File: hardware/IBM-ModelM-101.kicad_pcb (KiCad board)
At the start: 2 copper layers, 150 x 50 mm, 44 parts, among them J1 CONN-MOLEX-0670688000-USB-B, J2 KEYBOARD_ACTIVE_LINES, J3 KEYBOARD_INPUT_LINES, J4 CHASSIS_GROUND, J5 STATUS_LEDS, J6 DEBUG_FTDI, J7 JTAG, SW1 BOOT0, SW2 RESET, U1 TLV70233DBV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

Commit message: Adjusted output gerber naming
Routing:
- net GND: track 40.4 -> 33.1 mm
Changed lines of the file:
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@@
     (thickness 1.6)
     (drawings 93)
-    (tracks 501)
+    (tracks 499)
     (zones 0)
     (modules 44)
@@
   (page A4)
   (layers
-    (0 F.Cu signal hide)
-    (31 B.Cu signal hide)
+    (0 F.Cu signal)
+    (31 B.Cu signal)
     (32 B.Adhes user)
     (33 F.Adhes user)
@@
     (pcbplotparams
       (layerselection 0x010f0_80000001)
-      (usegerberextensions false)
+      (usegerberextensions true)
       (excludeedgelayer true)
       (linewidth 0.100000)
@@
       (plotinvisibletext false)
       (padsonsilk false)
-      (subtractmaskfromsilk false)
+      (subtractmaskfromsilk true)
       (outputformat 1)
       (mirror false)
@@
   (segment (start 151.869 46.851) (end 152.019 47.001) (width 0.254) (layer F.Cu) (net 1))
   (segment (start 158.508 48.895) (end 158.496 48.895) (width 0.254) (layer F.Cu) (net 1))
-  (segment (start 158.496 48.895) (end 153.913 48.895) (width 0.254) (layer F.Cu) (net 1))
-  (segment (start 153.913 48.895) (end 152.019 47.001) (width 0.254) (layer F.Cu) (net 1))
   (segment (start 161.556 48.514) (end 160.528 48.514) (width 0.254) (layer F.Cu) (net 2))
   (segment (start 160.02 48.26) (end 160.02 47.752) (width 0.254) (layer F.Cu) (net 2))

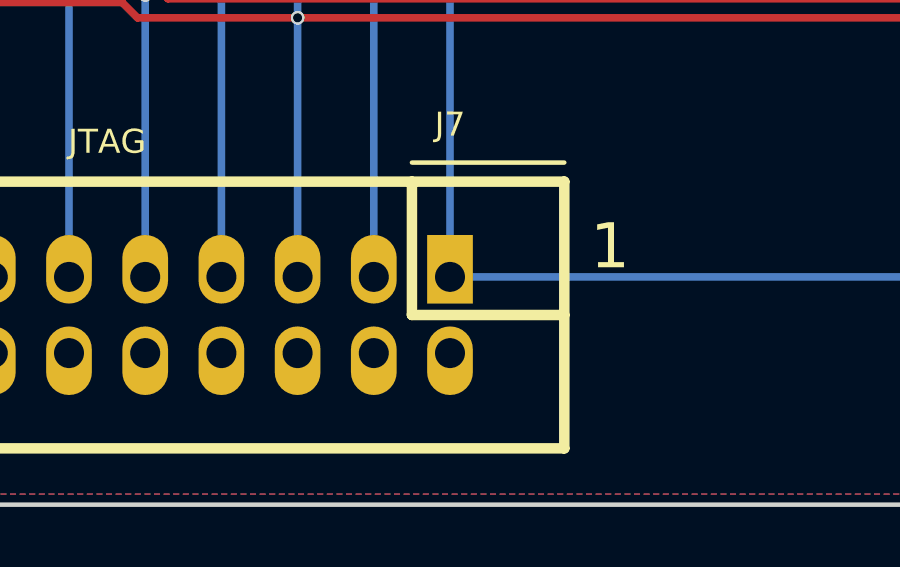
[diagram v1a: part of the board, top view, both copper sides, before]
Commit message: Converting to STM32F102
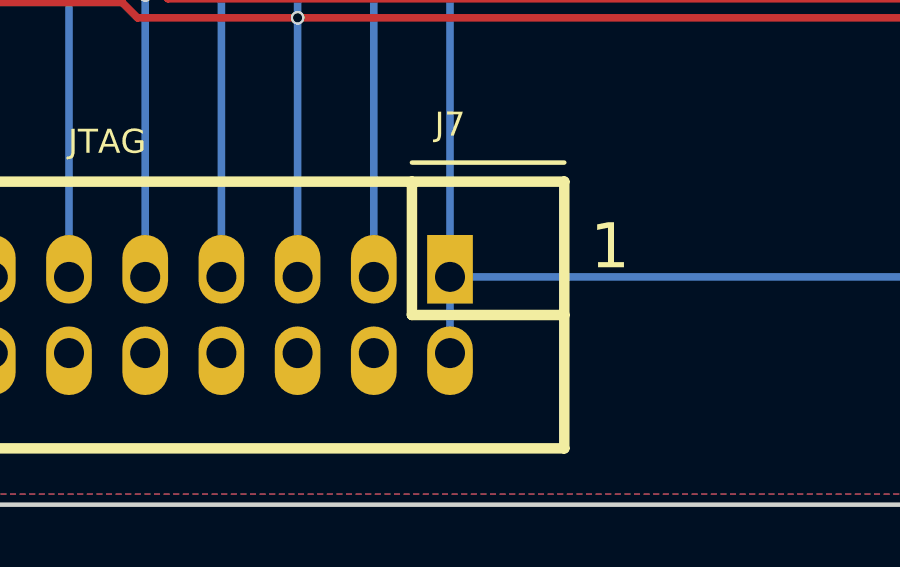
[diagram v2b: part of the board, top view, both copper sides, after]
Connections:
- J7 pad 2: GND -> +3V3
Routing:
- net +3V3: track 206.6 -> 209.2 mm
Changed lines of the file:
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@@
     (links 128)
     (no_connects 0)
-    (area 85.003799 20.793999 235.153801 76.755201)
+    (area 85.003799 26.605199 235.153801 76.755201)
     (thickness 1.6)
     (drawings 93)
-    (tracks 499)
+    (tracks 500)
     (zones 0)
     (modules 44)
@@
       (net 46 "Net-(J7-Pad19)"))
     (pad 2 thru_hole oval (at -11.43 -1.27 180) (size 1.524 2.286) (drill 1 (offset 0 -0.254)) (layers *.Cu *.Mask F.SilkS)
-      (net 1 GND))
+      (net 2 +3V3))
     (pad 4 thru_hole oval (at -8.89 -1.27 180) (size 1.524 2.286) (drill 1 (offset 0 -0.254)) (layers *.Cu *.Mask F.SilkS)
       (net 1 GND))
@@
       (xy 3.721004 -7.566813)) (layer F.SilkS) (width 0.01))
   )
+  (gr_text 3V3 (at 196.342 73.152 90) (layer B.SilkS)
+    (effects (font (size 0.762 0.762) (thickness 0.1905) italic) (justify right mirror))
+  )
   (gr_text 1 (at 136.398 33.02) (layer F.SilkS)
     (effects (font (size 1.5 1.5) (thickness 0.3)))
@@
     (effects (font (size 0.762 0.762) (thickness 0.1905) italic) (justify right mirror))
   )
-  (gr_text GND (at 196.342 73.152 90) (layer B.SilkS)
-    (effects (font (size 0.762 0.762) (thickness 0.1905) italic) (justify right mirror))
-  )
   (gr_text GND (at 168.402 73.152 90) (layer B.SilkS)
     (effects (font (size 0.762 0.762) (thickness 0.1905) italic) (justify right mirror))
@@
   (segment (start 151.869 46.851) (end 152.019 47.001) (width 0.254) (layer F.Cu) (net 1))
   (segment (start 158.508 48.895) (end 158.496 48.895) (width 0.254) (layer F.Cu) (net 1))
+  (segment (start 193.802 71.628) (end 193.802 69.088) (width 0.254) (layer B.Cu) (net 2) (status C00000))
   (segment (start 161.556 48.514) (end 160.528 48.514) (width 0.254) (layer F.Cu) (net 2))
   (segment (start 160.02 48.26) (end 160.02 47.752) (width 0.254) (layer F.Cu) (net 2))
@@
     (polygon
       (pts
-        (xy 195.072 73.66) (xy 169.418 73.66) (xy 169.418 70.358) (xy 195.326 70.358) (xy 195.326 73.66)
+        (xy 192.532 73.66) (xy 169.418 73.66) (xy 169.418 70.358) (xy 192.532 70.358) (xy 192.532 73.66)
       )
     )

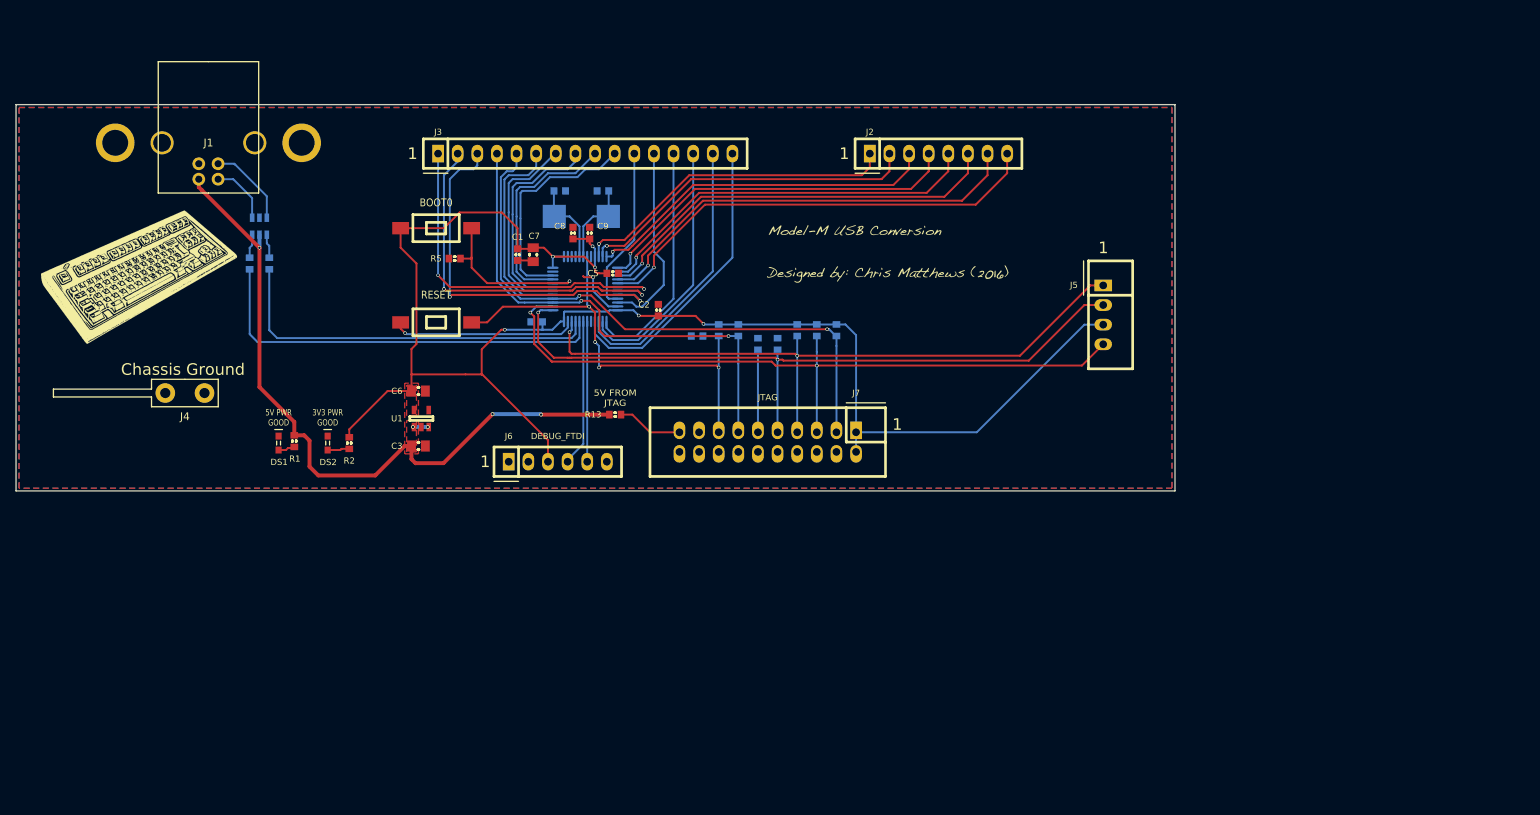
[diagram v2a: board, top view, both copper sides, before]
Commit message: Fixed key repeat code
Keys will now stop repeating if a modifier key is released or pressed.
Key repeat will pause 500msec before turning on.
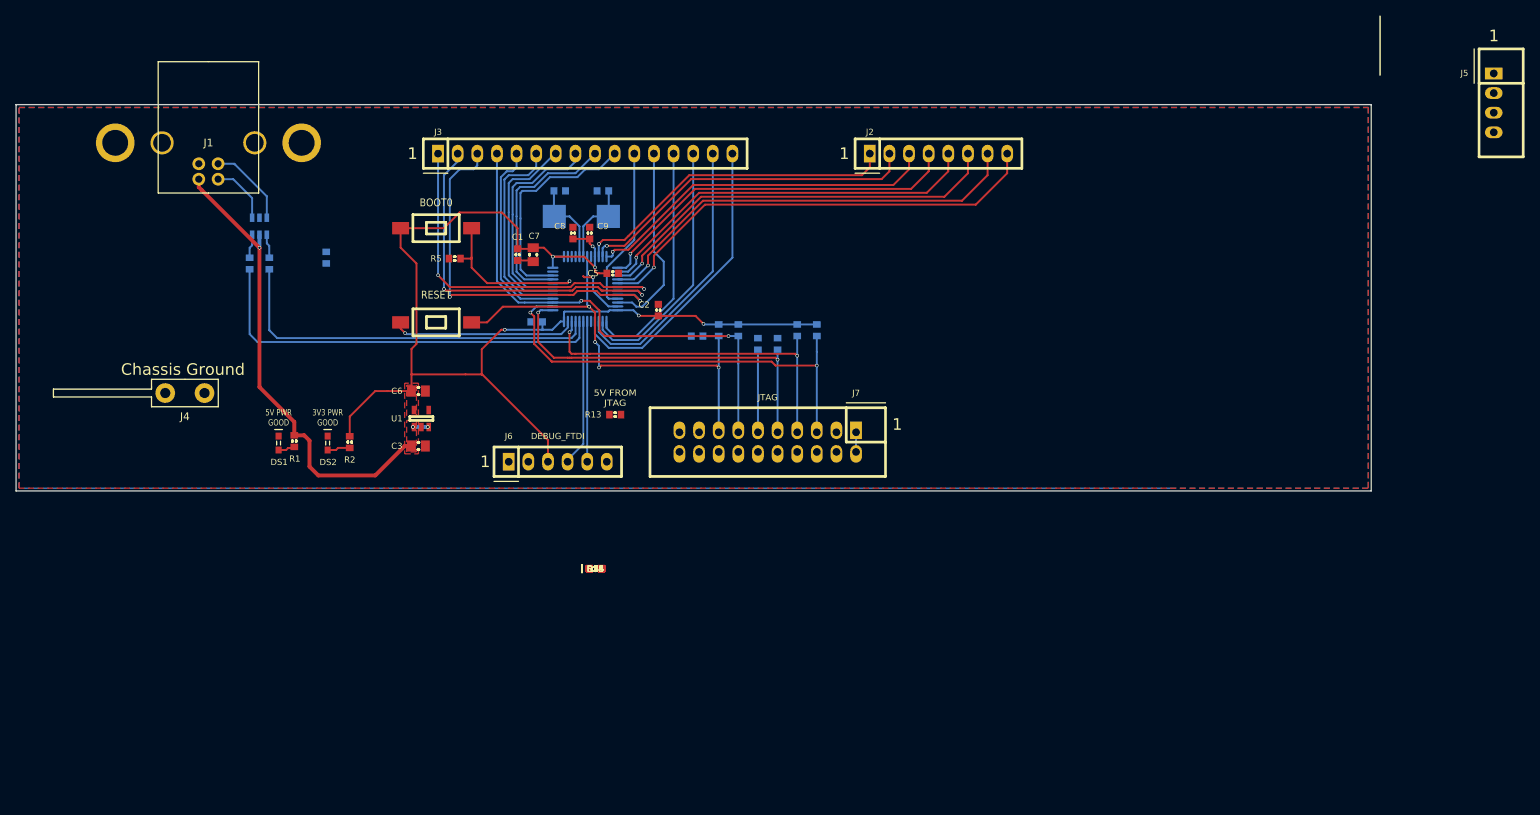
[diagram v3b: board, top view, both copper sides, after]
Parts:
- removed G***: LOGO, hardware:IBM-Model-M-Neg
- removed G***: LOGO, hardware:ModelMUsb
- added DS3, DS4, DS5: SCROLL LOCK, smd-semi:LED-0603, F.Cu at (160.1, 86.8)
- added R14, R15: 2K, IPC7351-Nominal:RESC1608X50, F.Cu at (160.1, 86.8)
- added R16: JTAG_3V3, IPC7351-Nominal:RESC1608X50, F.Cu at (160.1, 86.8)
- R1: value 1K -> 4K7
- R10: value 10K -> 2K
- R13: value 0R -> JTAG_5V
- R2: value 1K -> 2K
- R6: value 10K -> 1K5
- moved R6 66.7 mm to (125.2, 46.5)
- moved J5 57.5 mm to (276.3, 26.5)
- moved R2 0.14 mm to (128.3, 70.4)
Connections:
- J3 pad 5: /JNTRST -> Net-(J3-Pad5)
- J5 pad 1: /JTMS/SWDIO -> /~CAPS_LOCK_LED~
- J5 pad 2: /JTCK/SWCLK -> +3V3
- J5 pad 3: +3V3 -> /~SCROLL_LOCK_LED~
- J5 pad 4: /JTDI -> /~NUM_LOCK_LED~
- J6 pad 3: +3V3 -> Net-(J6-Pad3)
- J7 pad 1: +3V3 -> Net-(J7-Pad1)
- J7 pad 2: +3V3 -> Net-(J7-Pad1)
- J7 pad 3: /JNTRST -> GND
- R10 pad 1: Net-(J7-Pad11) -> Net-(DS3-Pad1)
- R10 pad 2: GND -> /~SCROLL_LOCK_LED~
- R6 pad 1: +3V3 -> /USB_EN
- R6 pad 2: /JNTRST -> Net-(DZ1-Pad4)
- U2 pad 2: Net-(U2-Pad2) -> /~NUM_LOCK_LED~
- U2 pad 29: Net-(U2-Pad29) -> /USB_EN
- U2 pad 3: Net-(U2-Pad3) -> /~SCROLL_LOCK_LED~
- U2 pad 4: Net-(U2-Pad4) -> /~CAPS_LOCK_LED~
- U2 pad 40: /JNTRST -> Net-(J3-Pad5)
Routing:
- net /JNTRST: track 76.8 -> 0.00 mm, vias 2 -> 0
- net +3V3: track 209.2 -> 148.6 mm
- net /JTCK/SWCLK: track 93.6 -> 48.4 mm
- net /JTMS/SWDIO: track 89.6 -> 46.2 mm
- net /JTDI: track 95.9 -> 57.7 mm
- net +5V: track 93.0 -> 62.8 mm, vias 5 -> 3
- net Net-(J3-Pad5): track 0.00 -> 25.3 mm
- net Net-(J7-Pad11): track 10.7 -> 0.00 mm
- net Net-(DS3-Pad1): track 0.00 -> 10.7 mm
- net Net-(J7-Pad19): track 8.77 -> 0.25 mm
- net Net-(J6-Pad3): track 0.00 -> 2.79 mm
- net Net-(J7-Pad1): track 0.00 -> 2.54 mm
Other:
- board size 150 x 50 mm -> 175.4 x 50 mm

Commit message: Updated schematic and PCB layout to fix errors in first revision.
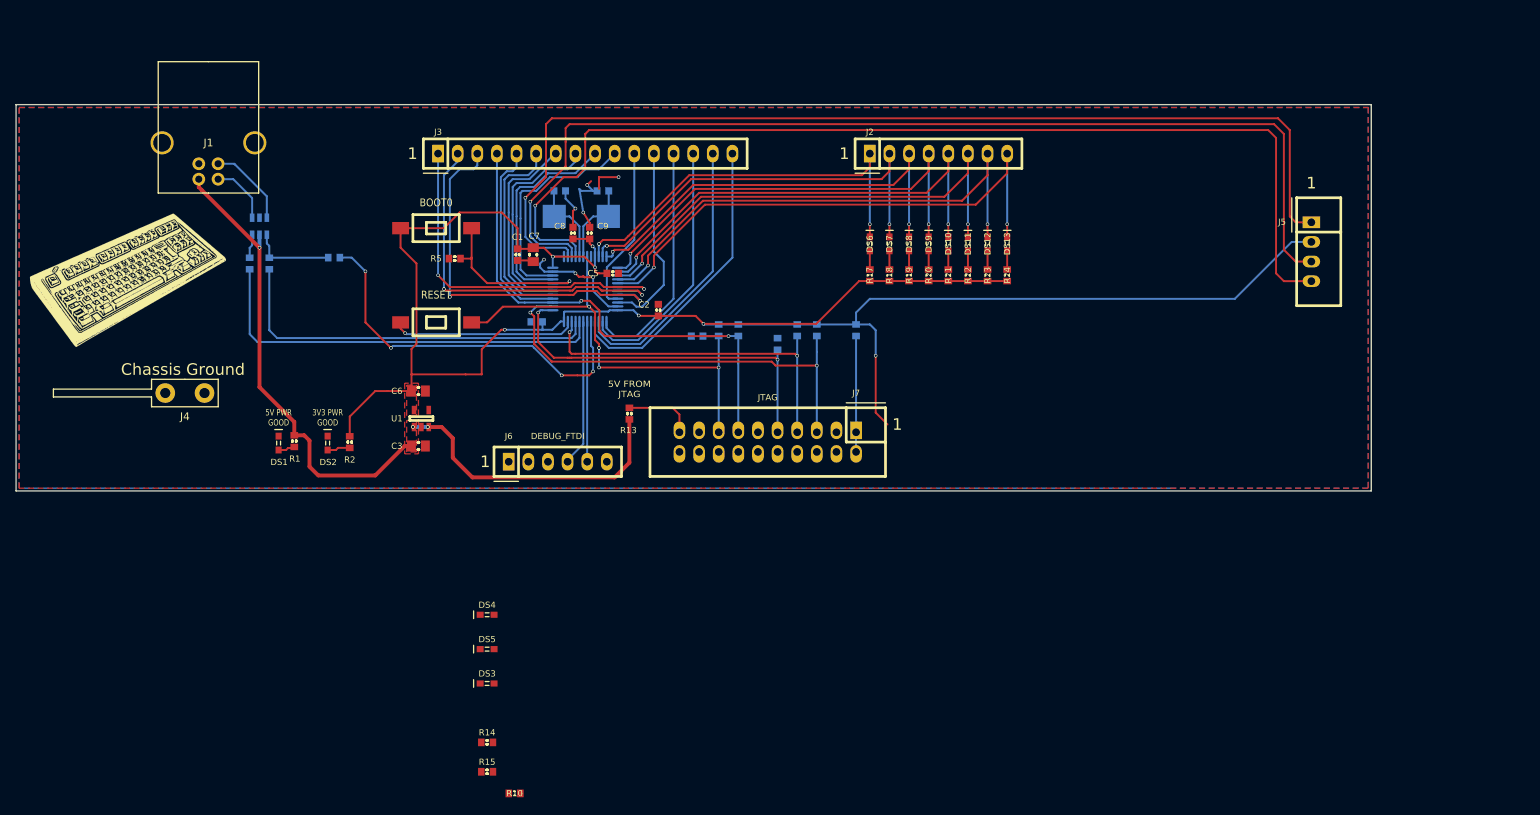
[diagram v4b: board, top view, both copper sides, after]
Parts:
- removed REF**: PTH-3MM-PLUS-SUPPORTED, mech:PTH-3MM-PLUS
- removed REF**: PTH-3MM-PLUS, mech:PTH-3MM-PLUS
- added DS10: PA4, smd-semi:LED-0603, F.Cu at (205.7, 44.7)
- added DS11: PA5, smd-semi:LED-0603, F.Cu at (208.3, 44.7)
- added DS12: PA6, smd-semi:LED-0603, F.Cu at (210.8, 44.7)
- added DS13: PA7, smd-semi:LED-0603, F.Cu at (213.4, 44.7)
- added DS6: PA0, smd-semi:LED-0603, F.Cu at (195.6, 44.7)
- added DS7: PA1, smd-semi:LED-0603, F.Cu at (198.1, 44.7)
- added DS8: PA2, smd-semi:LED-0603, F.Cu at (200.7, 44.7)
- added DS9: PA3, smd-semi:LED-0603, F.Cu at (203.2, 44.7)
- added G***: LOGO, hardware:IBM-Model-M-Neg, F.Cu at (99.6, 49.4)
- added R17: 2K, IPC7351-Nominal:RESC1608X50, F.Cu at (195.6, 48.8)
- added R18: 2K, IPC7351-Nominal:RESC1608X50, F.Cu at (198.1, 48.8)
- added R19: 2K, IPC7351-Nominal:RESC1608X50, F.Cu at (200.7, 48.8)
- added R20: 2K, IPC7351-Nominal:RESC1608X50, F.Cu at (203.2, 48.8)
- added R21: 2K, IPC7351-Nominal:RESC1608X50, F.Cu at (205.7, 48.8)
- added R22: 2K, IPC7351-Nominal:RESC1608X50, F.Cu at (208.3, 48.8)
- added R23: 2K, IPC7351-Nominal:RESC1608X50, F.Cu at (210.8, 48.8)
- added R24: 2K, IPC7351-Nominal:RESC1608X50, F.Cu at (213.4, 48.8)
- DS4: value SCROLL LOCK -> CAPS LOCK
- DS5: value SCROLL LOCK -> NUM LOCK
- R10: moved to F.Cu
- R16: moved to B.Cu
- moved R10 66.1 mm to (149.6, 115.8), turned to 0 degrees
- moved R16 45.7 mm to (193.8, 55.9), turned to 90 degrees
- moved J5 30.5 mm to (252.7, 45.7)
- moved R15 29.8 mm to (146.1, 113.0)
- moved R14 26.5 mm to (146.1, 109.2)
- moved DS3 20.4 mm to (146.1, 101.6)
- moved DS5 17.5 mm to (146.1, 97.2)
- moved DS4 15.2 mm to (146.1, 92.7)
- moved R13 1.85 mm to (164.5, 66.7), turned to 270 degrees
- moved R6 1.02 mm to (126.2, 46.5), turned to 180 degrees
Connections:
- net Net-(J2-Pad1) renamed /PA0_IO
- net Net-(J2-Pad2) renamed /PA1_IO
- net Net-(J2-Pad3) renamed /PA2_IO
- net Net-(J2-Pad4) renamed /PA3_IO
- net Net-(J2-Pad5) renamed /PA4_IO
- net Net-(J2-Pad6) renamed /PA5_IO
- net Net-(J2-Pad7) renamed /PA6_IO
- net Net-(J2-Pad8) renamed /PA7_IO
- U2 pad 2: /~NUM_LOCK_LED~ -> /~CAPS_LOCK_LED~
- U2 pad 4: /~CAPS_LOCK_LED~ -> /~NUM_LOCK_LED~
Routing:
- net /~NUM_LOCK_LED~: track 0.00 -> 136.5 mm, vias 0 -> 1
- net /~SCROLL_LOCK_LED~: track 0.00 -> 135.8 mm, vias 0 -> 1
- net /~CAPS_LOCK_LED~: track 0.00 -> 134.2 mm, vias 0 -> 1
- net +3V3: track 148.6 -> 263.1 mm, vias 6 -> 7
- net /USB_EN: track 0.00 -> 50.0 mm, vias 0 -> 4
- net +5V: track 62.8 -> 99.3 mm
- net GND: track 33.1 -> 60.0 mm, vias 2 -> 8
- net Net-(J7-Pad1): track 2.54 -> 15.0 mm
- net /PA6_IO: track 57.0 -> 67.8 mm, vias 1 -> 2
- net /PA5_IO: track 53.9 -> 64.7 mm, vias 1 -> 2
- net /PA4_IO: track 51.1 -> 61.8 mm, vias 1 -> 2
- net /PA3_IO: track 48.5 -> 59.2 mm, vias 1 -> 2
- net /PA1_IO: track 44.6 -> 55.4 mm, vias 1 -> 2
- net /PA0_IO: track 42.6 -> 53.4 mm, vias 1 -> 2
- net /PA7_IO: track 59.7 -> 70.5 mm, vias 1 -> 2
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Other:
- board text added: "3V3 FROM JTAG"
- board text added: "DO NOT LAY OUT"

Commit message: Updated copyright information.
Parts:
- added G***: LOGO, hardware:ModelMUsb, F.Cu at (231.6, 69.6)
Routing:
- net GND: track 60.0 -> 55.9 mm, vias 8 -> 7
- net (no net): track 0.00 -> 4.06 mm, vias 0 -> 1
